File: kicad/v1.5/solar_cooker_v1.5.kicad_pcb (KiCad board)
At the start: 2 copper layers, 155.4 x 77.1 mm, 17 parts, among them U1 microSD, U10 GPS, U2 clock_module, U3 anemometer, U4 AM2315, U5 BME680, U6 PT100, U7 pyranometer, U8 PT100, U9 PT100

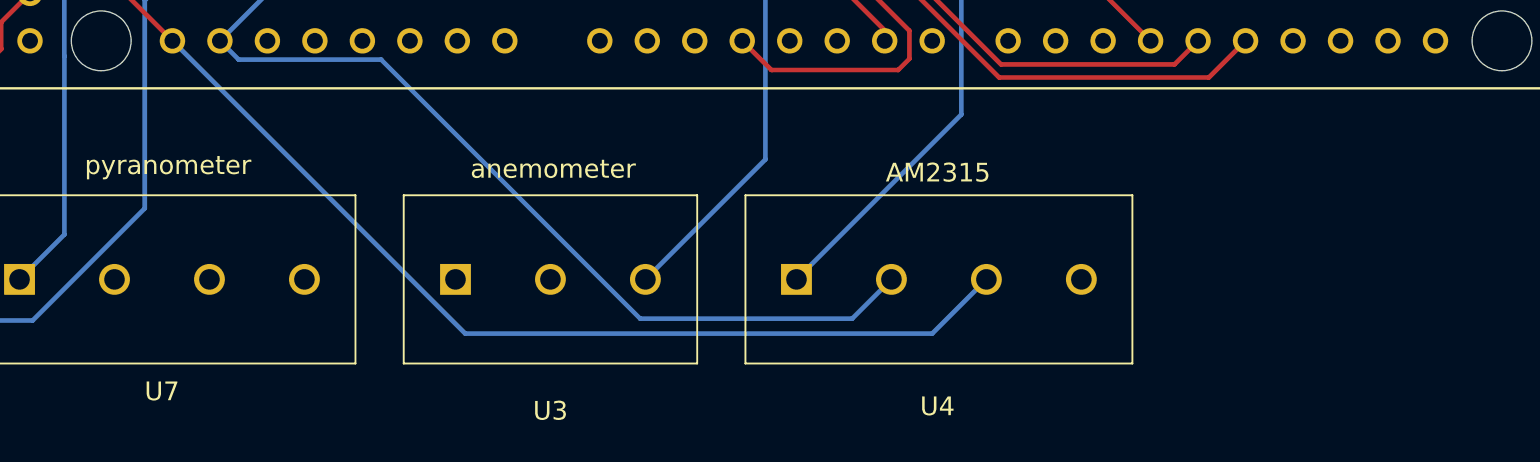
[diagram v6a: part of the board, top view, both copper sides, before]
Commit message: converter scheme and footprint added
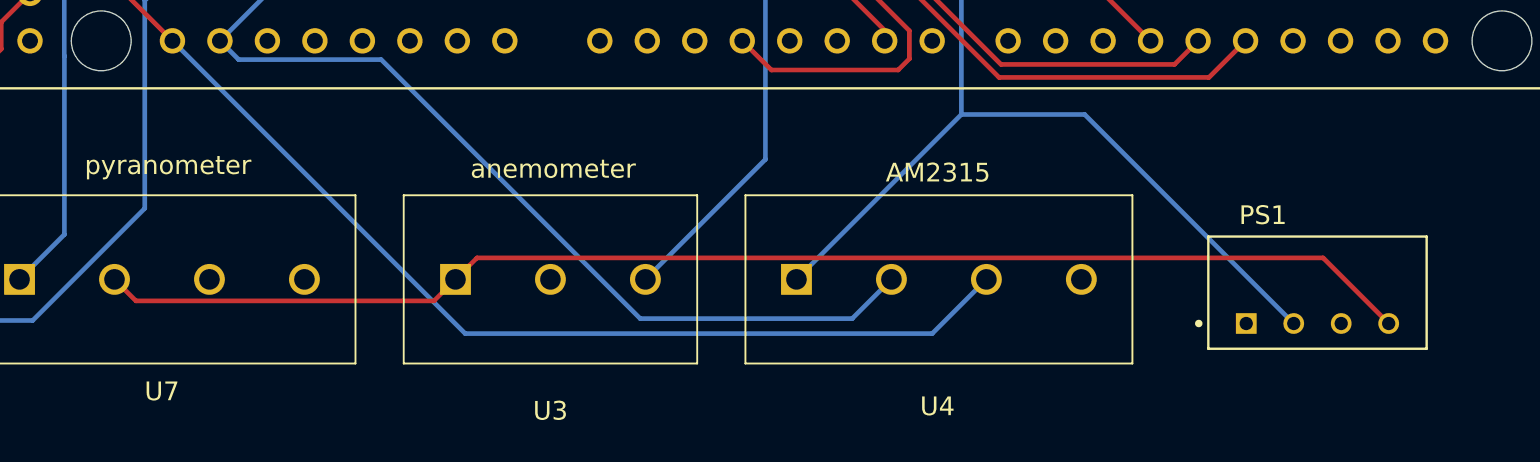
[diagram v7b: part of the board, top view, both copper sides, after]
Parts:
- added PS1: TBA_1-0519, TBA_1-0519:CONV_TBA_1-0519, F.Cu at (214.6, 148.2)
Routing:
- net +9V: track 0.00 -> 71.0 mm
- net +5V: track 220.7 -> 243.1 mm
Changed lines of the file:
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@@
   (net 105 "unconnected-(U9-RDY-Pad1)")
   (net 106 "unconnected-(U9-3V3-Pad6)")
+  (net 107 "unconnected-(PS1--VOUT-Pad3)")
   (footprint "custom_components:BME680" (layer "F.Cu")
     (at 113.9246 150.975)
@@
     (pad "6" thru_hole circle (at 6.32 -8.1) (size 1.65 1.65) (drill 1.1) (layers "*.Cu" "*.Mask")
       (net 15 "/D6") (pinfunction "CS") (pintype "input"))
+  )
+  (footprint "TBA_1-0519:CONV_TBA_1-0519" (layer "F.Cu")
+    (at 214.63 148.21)
+    (property "MANUFACTURER" "Traco Power")
+    (property "MAXIMUM_PACKAGE_HEIGHT" "10.15mm")
+    (property "PARTREV" "April 19, 2021")
+    (property "STANDARD" "Manufacturer Recommendations")
+    (property "Sheetfile" "solar_cooker_v1.5.kicad_sch")
+    (property "Sheetname" "")
+    (attr through_hole)
+    (fp_text reference "PS1" (at -2.915 -4.135) (layer "F.SilkS")
+        (effects (font (size 1 1) (thickness 0.15)))
+    )
+    (fp_text value "TBA_1-0519" (at 3.435 4.135) (layer "F.Fab")
+        (effects (font (size 1 1) (thickness 0.15)))
+    )
+    (fp_line (start -5.84 -3) (end 5.84 -3)
+      (stroke (width 0.127) (type solid)) (layer "F.SilkS"))
+    (fp_line (start -5.84 3) (end -5.84 -3)
+      (stroke (width 0.127) (type solid)) (layer "F.SilkS"))
+    (fp_line (start 5.84 -3) (end 5.84 3)
+      (stroke (width 0.127) (type solid)) (layer "F.SilkS"))
+    (fp_line (start 5.84 3) (end -5.84 3)
+      (stroke (width 0.127) (type solid)) (layer "F.SilkS"))
+    (fp_circle (center -6.35 1.65) (end -6.25 1.65)
+      (stroke (width 0.2) (type solid)) (fill none) (layer "F.SilkS"))
+    (fp_line (start -6.09 -3.25) (end -6.09 3.25)
+      (stroke (width 0.05) (type solid)) (layer "F.CrtYd"))
+    (fp_line (start -6.09 3.25) (end 6.09 3.25)
+      (stroke (width 0.05) (type solid)) (layer "F.CrtYd"))
+    (fp_line (start 6.09 -3.25) (end -6.09 -3.25)
+      (stroke (width 0.05) (type solid)) (layer "F.CrtYd"))
+    (fp_line (start 6.09 3.25) (end 6.09 -3.25)
+      (stroke (width 0.05) (type solid)) (layer "F.CrtYd"))
+    (fp_line (start -5.84 -3) (end 5.84 -3)
+      (stroke (width 0.127) (type solid)) (layer "F.Fab"))
+    (fp_line (start -5.84 3) (end -5.84 -3)
+      (stroke (width 0.127) (type solid)) (layer "F.Fab"))
+    (fp_line (start 5.84 -3) (end 5.84 3)
+      (stroke (width 0.127) (type solid)) (layer "F.Fab"))
+    (fp_line (start 5.84 3) (end -5.84 3)
+      (stroke (width 0.127) (type solid)) (layer "F.Fab"))
+    (fp_circle (center -6.35 1.65) (end -6.25 1.65)
+      (stroke (width 0.2) (type solid)) (fill none) (layer "F.Fab"))
+    (pad "1" thru_hole rect (at -3.81 1.65) (size 1.11 1.11) (drill 0.71) (layers "*.Cu" "*.Mask")
+      (net 2 "GND") (pinfunction "-VIN(GND)") (pintype "input"))
+    (pad "2" thru_hole circle (at -1.27 1.65) (size 1.11 1.11) (drill 0.71) (layers "*.Cu" "*.Mask")
+      (net 10 "+5V") (pinfunction "+VIN(VCC)") (pintype "input"))
+    (pad "3" thru_hole circle (at 1.27 1.65) (size 1.11 1.11) (drill 0.71) (layers "*.Cu" "*.Mask")
+      (net 107 "unconnected-(PS1--VOUT-Pad3)") (pinfunction "-VOUT") (pintype "output"))
+    (pad "4" thru_hole circle (at 3.81 1.65) (size 1.11 1.11) (drill 0.71) (layers "*.Cu" "*.Mask")
+      (net 13 "+9V") (pinfunction "+VOUT") (pintype "output"))
   )
   (footprint "custom_components:PT100" (layer "F.Cu")
@@
         (effects (font (size 1 1) (thickness 0.15)))
     )
-    (fp_text value "500SSP1S2M2QEA" (at 4.445 4.445 180) (layer "F.Fab") hide
+    (fp_text value "500SSP1S2M2QEA" (at 4.445 4.445 180) (layer "F.Fab")
         (effects (font (size 1 1) (thickness 0.15)))
     )
@@
   (segment (start 135.4246 147.5) (end 133.6746 149.25) (width 0.25) (layer "B.Cu") (net 10))
   (segment (start 111.76 147.32) (end 106.68 147.32) (width 0.25) (layer "B.Cu") (net 10))
+  (segment (start 202.18 138.68) (end 195.58 138.68) (width 0.25) (layer "B.Cu") (net 10))
+  (segment (start 213.36 149.86) (end 202.18 138.68) (width 0.25) (layer "B.Cu") (net 10))
   (segment (start 133.6746 149.25) (end 129.786396 149.25) (width 0.25) (layer "B.Cu") (net 10))
   (segment (start 114.885946 147.32) (end 111.76 147.32) (width 0.25) (layer "B.Cu") (net 10))
@@
   (segment (start 196.92 147.5) (end 194.02 150.4) (width 0.25) (layer "B.Cu") (net 12))
   (segment (start 194.02 150.4) (end 169.04 150.4) (width 0.25) (layer "B.Cu") (net 12))
+  (segment (start 218.44 149.86) (end 214.93 146.35) (width 0.25) (layer "F.Cu") (net 13))
+  (segment (start 167.37 148.65) (end 151.43 148.65) (width 0.25) (layer "F.Cu") (net 13))
+  (segment (start 214.93 146.35) (end 169.67 146.35) (width 0.25) (layer "F.Cu") (net 13))
+  (segment (start 169.67 146.35) (end 168.52 147.5) (width 0.25) (layer "F.Cu") (net 13))
+  (segment (start 151.43 148.65) (end 150.28 147.5) (width 0.25) (layer "F.Cu") (net 13))
+  (segment (start 168.52 147.5) (end 167.37 148.65) (width 0.25) (layer "F.Cu") (net 13))
   (segment (start 185.100129 90.319871) (end 188.94 86.48) (width 0.25) (layer "B.Cu") (net 14))
   (segment (start 185.100129 141.079871) (end 185.100129 90.319871) (width 0.25) (layer "B.Cu") (net 14))

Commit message: drc fix
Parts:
- PS1: footprint TBA_1-0519:CONV_TBA_1-0519 -> dcdc convertor:CONV_TBA_1-0519
- moved PS1 89.1 mm to (127.1, 131.3)
- moved D1 3.53 mm to (111.6, 130.6)
- moved D2 3.53 mm to (111.6, 135.6)
- moved R1 3.53 mm to (123.6, 153.3)
- moved R2 3.53 mm to (105.5, 130.6)
- moved R3 3.53 mm to (105.5, 135.6)
- moved S1 3.53 mm to (127.5, 146.0)
- moved U1 3.53 mm to (118.7, 107.7)
- moved U10 3.53 mm to (90.6, 103.9)
- moved U2 3.53 mm to (89.3, 141.0)
- moved U5 3.53 mm to (110.7, 149.5)
- moved U6 3.53 mm to (57.8, 92.8)
- moved U8 3.53 mm to (57.8, 119.3)
- moved U9 3.53 mm to (57.8, 145.8)
- moved A1 3.53 mm to (185.7, 109.1)
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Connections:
- A1 pad 5V_3: unconnected-(A1-+5V_3-Pad5V_3) -> +5V
- A1 pad GND2: unconnected-(A1-PadGND2) -> GND
- A1 pad GND3: unconnected-(A1-PadGND3) -> GND
- A1 pad GND4: unconnected-(A1-PadGND4) -> GND
- A1 pad GND5: unconnected-(A1-PadGND5) -> GND
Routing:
- net GND: track 0.00 -> 29.8 mm, vias 0 -> 28
- net +9V: track 71.0 -> 47.4 mm, vias 0 -> 1
- net /D22: track 41.1 -> 61.9 mm
- net /SDA: track 193.1 -> 201.7 mm
- net +5V: track 243.1 -> 248.3 mm, vias 2 -> 5
- net /MOSI: track 155.9 -> 157.7 mm
- net /D12: track 140.9 -> 142.4 mm
- net /D13: track 148.1 -> 149.6 mm
- net /MISO: track 157.4 -> 158.5 mm
- net /D6: track 92.9 -> 93.9 mm
- net /SCK: track 179.0 -> 179.7 mm
- added copper zone on B.Cu, net GND
- added copper zone on F.Cu, net GND
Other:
- board text added: "external cabels"
- board text removed: "external kabels"
